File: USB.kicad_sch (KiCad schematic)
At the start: 51 parts, among them J3 USB_C_Receptacle_USB2.0, J4 USB_A_Stacked, Q4 BC817, U10 TPD4EUSB30, U4 CP2102N-Axx-xQFN24, U5 FSUSB30MUX, U6 FSUSB30MUX, U7 FE1.1, U8 TPD4EUSB30, U9 AP2191W, Y1 12MHz{slash}10pF

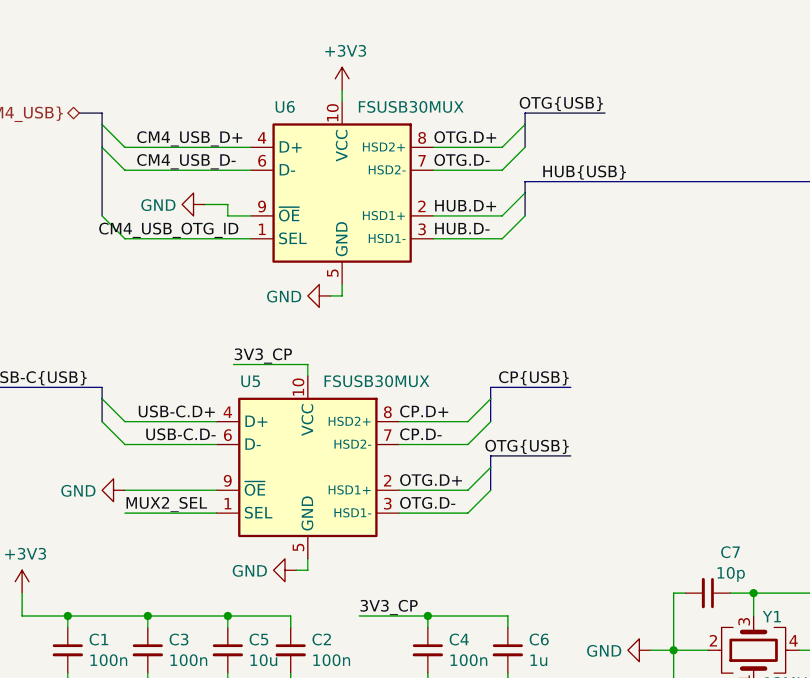
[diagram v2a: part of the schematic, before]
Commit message: Fix FSUSB30 Symbol and routing
Additionally a cap was added to U27.

Signed-off-by: Dominik Sliwa <dominik@sliwa.io>
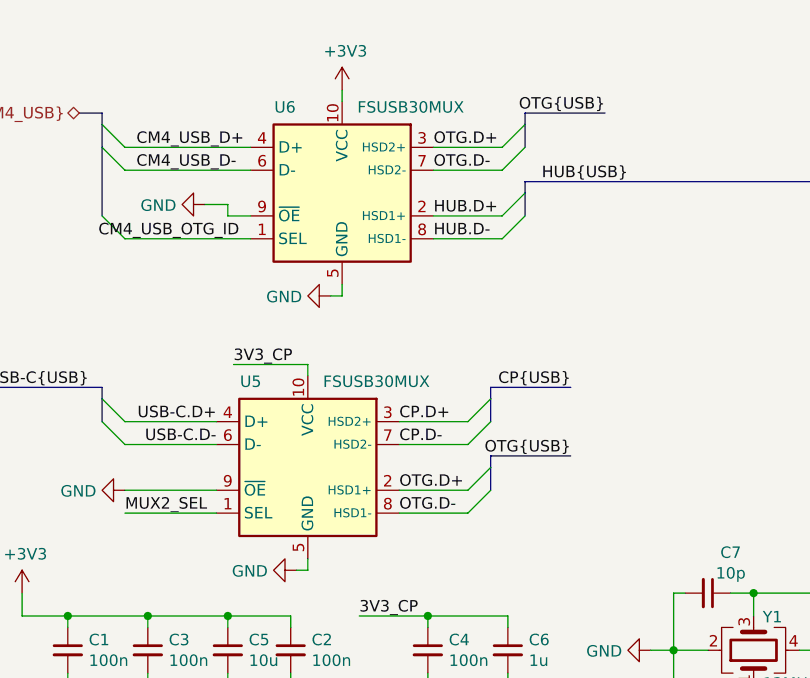
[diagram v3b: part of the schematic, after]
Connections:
- net CP.D+: now also U5.3 (HSD2+); no longer U5.8 (HSD2+)
- net HUB.D-: now also U6.8 (HSD1-); no longer U6.3 (HSD1-)
- net OTG.D+: now also U6.3 (HSD2+); no longer U6.8 (HSD2+)
- net OTG.D-: now also U5.8 (HSD1-); no longer U5.3 (HSD1-)
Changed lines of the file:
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@@
-(kicad_sch (version 20210621) (generator eeschema)
+(kicad_sch (version 20211123) (generator eeschema)
   (paper "A4")
   (title_block
@@
   (bus_alias "CM4_USB" (members "CM4_USB_D+" "CM4_USB_D-" "CM4_USB_OTG_ID"))
   (bus_alias "USB" (members "D+" "D-"))
-  (junction (at 40.64 88.9) (diameter 0.9144) (color 0 0 0 0))
-  (junction (at 92.075 154.305) (diameter 0.9144) (color 0 0 0 0))
-  (junction (at 143.51 29.21) (diameter 0.9144) (color 0 0 0 0))
-  (junction (at 22.86 80.01) (diameter 0.9144) (color 0 0 0 0))
-  (junction (at 228.6 42.545) (diameter 0) (color 0 0 0 0))
-  (junction (at 233.045 71.12) (diameter 0.9144) (color 0 0 0 0))
-  (junction (at 62.865 88.9) (diameter 0.9144) (color 0 0 0 0))
-  (junction (at 213.36 48.895) (diameter 0) (color 0 0 0 0))
-  (junction (at 92.075 139.065) (diameter 0.9144) (color 0 0 0 0))
-  (junction (at 152.4 29.21) (diameter 0.9144) (color 0 0 0 0))
-  (junction (at 274.32 123.19) (diameter 0.9144) (color 0 0 0 0))
-  (junction (at 144.78 100.33) (diameter 0.9144) (color 0 0 0 0))
-  (junction (at 238.125 34.29) (diameter 0.9144) (color 0 0 0 0))
-  (junction (at 215.265 59.69) (diameter 0.9144) (color 0 0 0 0))
-  (junction (at 222.885 89.535) (diameter 0.9144) (color 0 0 0 0))
-  (junction (at 62.865 80.01) (diameter 0.9144) (color 0 0 0 0))
-  (junction (at 224.155 71.12) (diameter 0.9144) (color 0 0 0 0))
-  (junction (at 149.86 29.21) (diameter 0.9144) (color 0 0 0 0))
-  (junction (at 215.265 71.12) (diameter 0.9144) (color 0 0 0 0))
-  (junction (at 47.625 88.9) (diameter 0.9144) (color 0 0 0 0))
-  (junction (at 36.83 194.945) (diameter 0.9144) (color 0 0 0 0))
-  (junction (at 31.75 80.01) (diameter 0.9144) (color 0 0 0 0))
-  (junction (at 119.38 72.39) (diameter 0.9144) (color 0 0 0 0))
-  (junction (at 40.64 80.01) (diameter 0.9144) (color 0 0 0 0))
-  (junction (at 135.89 139.7) (diameter 0.9144) (color 0 0 0 0))
-  (junction (at 163.83 29.21) (diameter 0.9144) (color 0 0 0 0))
-  (junction (at 92.075 163.195) (diameter 0.9144) (color 0 0 0 0))
-  (junction (at 119.38 55.88) (diameter 0.9144) (color 0 0 0 0))
-  (junction (at 234.315 34.29) (diameter 0) (color 0 0 0 0))
-  (junction (at 224.155 59.69) (diameter 0.9144) (color 0 0 0 0))
-  (junction (at 99.06 77.47) (diameter 0.9144) (color 0 0 0 0))
-  (junction (at 90.17 83.82) (diameter 0.9144) (color 0 0 0 0))
-  (junction (at 240.665 71.12) (diameter 0.9144) (color 0 0 0 0))
-  (junction (at 24.765 187.325) (diameter 0.9144) (color 0 0 0 0))
-  (junction (at 234.315 42.545) (diameter 0) (color 0 0 0 0))
-  (junction (at 92.075 147.955) (diameter 0.9144) (color 0 0 0 0))
-  (junction (at 22.86 88.9) (diameter 0.9144) (color 0 0 0 0))
-  (junction (at 31.75 88.9) (diameter 0.9144) (color 0 0 0 0))
-  (junction (at 135.89 144.78) (diameter 0.9144) (color 0 0 0 0))
-  (junction (at 170.18 69.85) (diameter 0.9144) (color 0 0 0 0))
-  (junction (at 224.155 98.425) (diameter 0.9144) (color 0 0 0 0))
-  (junction (at 230.505 34.29) (diameter 0.9144) (color 0 0 0 0))
-  (junction (at 173.99 19.685) (diameter 0.9144) (color 0 0 0 0))
-  (junction (at 123.19 132.08) (diameter 0.9144) (color 0 0 0 0))
-  (junction (at 240.665 59.69) (diameter 0.9144) (color 0 0 0 0))
-  (junction (at 53.975 179.705) (diameter 0.9144) (color 0 0 0 0))
-  (junction (at 163.83 19.685) (diameter 0.9144) (color 0 0 0 0))
-  (junction (at 234.315 24.13) (diameter 0.9144) (color 0 0 0 0))
-  (junction (at 99.06 90.17) (diameter 0.9144) (color 0 0 0 0))
-  (junction (at 233.045 59.69) (diameter 0.9144) (color 0 0 0 0))
+  (junction (at 215.265 71.12) (diameter 0.9144) (color 0 0 0 0)
+  )
+  (junction (at 31.75 80.01) (diameter 0.9144) (color 0 0 0 0)
+  )
+  (junction (at 92.075 139.065) (diameter 0.9144) (color 0 0 0 0)
+  )
+  (junction (at 40.64 80.01) (diameter 0.9144) (color 0 0 0 0)
+  )
+  (junction (at 149.86 29.21) (diameter 0.9144) (color 0 0 0 0)
+  )
+  (junction (at 213.36 48.895) (diameter 0) (color 0 0 0 0)
+  )
+  (junction (at 22.86 88.9) (diameter 0.9144) (color 0 0 0 0)
+  )
+  (junction (at 215.265 59.69) (diameter 0.9144) (color 0 0 0 0)
+  )
+  (junction (at 233.045 71.12) (diameter 0.9144) (color 0 0 0 0)
+  )
+  (junction (at 119.38 55.88) (diameter 0.9144) (color 0 0 0 0)
+  )
+  (junction (at 24.765 187.325) (diameter 0.9144) (color 0 0 0 0)
+  )
+  (junction (at 240.665 59.69) (diameter 0.9144) (color 0 0 0 0)
+  )
+  (junction (at 53.975 179.705) (diameter 0.9144) (color 0 0 0 0)
+  )
+  (junction (at 234.315 24.13) (diameter 0.9144) (color 0 0 0 0)
+  )
+  (junction (at 92.075 154.305) (diameter 0.9144) (color 0 0 0 0)
+  )
+  (junction (at 224.155 71.12) (diameter 0.9144) (color 0 0 0 0)
+  )
+  (junction (at 92.075 147.955) (diameter 0.9144) (color 0 0 0 0)
+  )
+  (junction (at 228.6 42.545) (diameter 0) (color 0 0 0 0)
+  )
+  (junction (at 173.99 19.685) (diameter 0.9144) (color 0 0 0 0)
+  )
+  (junction (at 234.315 42.545) (diameter 0) (color 0 0 0 0)
+  )
+  (junction (at 230.505 34.29) (diameter 0.9144) (color 0 0 0 0)
+  )
+  (junction (at 135.89 144.78) (diameter 0.9144) (color 0 0 0 0)
+  )
+  (junction (at 143.51 29.21) (diameter 0.9144) (color 0 0 0 0)
+  )
+  (junction (at 233.045 59.69) (diameter 0.9144) (color 0 0 0 0)
+  )
+  (junction (at 62.865 88.9) (diameter 0.9144) (color 0 0 0 0)
+  )
+  (junction (at 222.885 89.535) (diameter 0.9144) (color 0 0 0 0)
+  )
+  (junction (at 144.78 100.33) (diameter 0.9144) (color 0 0 0 0)
+  )
+  (junction (at 90.17 83.82) (diameter 0.9144) (color 0 0 0 0)
+  )
+  (junction (at 99.06 90.17) (diameter 0.9144) (color 0 0 0 0)
+  )
+  (junction (at 119.38 72.39) (diameter 0.9144) (color 0 0 0 0)
+  )
+  (junction (at 152.4 29.21) (diameter 0.9144) (color 0 0 0 0)
+  )
+  (junction (at 123.19 132.08) (diameter 0.9144) (color 0 0 0 0)
+  )
+  (junction (at 135.89 139.7) (diameter 0.9144) (color 0 0 0 0)
+  )
+  (junction (at 40.64 88.9) (diameter 0.9144) (color 0 0 0 0)
+  )
+  (junction (at 170.18 69.85) (diameter 0.9144) (color 0 0 0 0)
+  )
+  (junction (at 238.125 34.29) (diameter 0.9144) (color 0 0 0 0)
+  )
+  (junction (at 31.75 88.9) (diameter 0.9144) (color 0 0 0 0)
+  )
+  (junction (at 99.06 77.47) (diameter 0.9144) (color 0 0 0 0)
+  )
+  (junction (at 240.665 71.12) (diameter 0.9144) (color 0 0 0 0)
+  )
+  (junction (at 224.155 59.69) (diameter 0.9144) (color 0 0 0 0)
+  )
+  (junction (at 47.625 88.9) (diameter 0.9144) (color 0 0 0 0)
+  )
+  (junction (at 274.32 123.19) (diameter 0.9144) (color 0 0 0 0)
+  )
+  (junction (at 163.83 19.685) (diameter 0.9144) (color 0 0 0 0)
+  )
+  (junction (at 92.075 163.195) (diameter 0.9144) (color 0 0 0 0)
+  )
+  (junction (at 36.83 194.945) (diameter 0.9144) (color 0 0 0 0)
+  )
+  (junction (at 224.155 98.425) (diameter 0.9144) (color 0 0 0 0)
+  )
+  (junction (at 163.83 29.21) (diameter 0.9144) (color 0 0 0 0)
+  )
+  (junction (at 234.315 34.29) (diameter 0) (color 0 0 0 0)
+  )
+  (junction (at 62.865 80.01) (diameter 0.9144) (color 0 0 0 0)
+  )
+  (junction (at 22.86 80.01) (diameter 0.9144) (color 0 0 0 0)
+  )
   (no_connect (at 167.64 77.47))
   (no_connect (at 138.43 153.67))
@@
     (pin "3")
   )
-  (symbol (lib_id "Amber:FSUSB30MUX") (at 53.34 33.02 0) (unit 1)
+  (symbol (lib_name "FSUSB30MUX_1") (lib_id "Amber:FSUSB30MUX") (at 53.34 33.02 0) (unit 1)
     (in_bom yes) (on_board yes)
     (property "Reference" "U6" (id 0) (at 46.99 23.495 0))

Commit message: Rename Amber to Yellow everywhere
Signed-off-by: Stefan Agner <stefan@agner.ch>
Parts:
- J4: symbol Amber:USB_A_Stacked -> Yellow:USB_A_Stacked
- U10, U8: symbol Amber:TPD4EUSB30 -> Yellow:TPD4EUSB30
- U5, U6: symbol Amber:FSUSB30MUX -> Yellow:FSUSB30MUX
- U7: symbol Amber:FE1.1 -> Yellow:FE1.1
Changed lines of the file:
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@@
     (pin "3")
   )
-  (symbol (lib_name "FSUSB30MUX_1") (lib_id "Amber:FSUSB30MUX") (at 53.34 33.02 0) (unit 1)
+  (symbol (lib_name "FSUSB30MUX_1") (lib_id "Yellow:FSUSB30MUX") (at 53.34 33.02 0) (unit 1)
     (in_bom yes) (on_board yes)
     (property "Reference" "U6" (id 0) (at 46.99 23.495 0))
@@
     (pin "1")
   )
-  (symbol (lib_name "Amber:USB_A_Stacked_1") (lib_id "Amber:USB_A_Stacked") (at 264.16 81.28 0) (mirror y) (unit 1)
+  (symbol (lib_name "Yellow:USB_A_Stacked_1") (lib_id "Yellow:USB_A_Stacked") (at 264.16 81.28 0) (mirror y) (unit 1)
     (in_bom yes) (on_board yes)
     (property "Reference" "J4" (id 0) (at 261.62 68.58 0))
@@
     (pin "2")
   )
-  (symbol (lib_id "Amber:USB_A_Stacked") (at 264.16 113.03 0) (mirror y) (unit 2)
+  (symbol (lib_id "Yellow:USB_A_Stacked") (at 264.16 113.03 0) (mirror y) (unit 2)
     (in_bom yes) (on_board yes)
     (property "Reference" "J4" (id 0) (at 261.62 100.33 0))
@@
     (pin "2")
   )
-  (symbol (lib_id "Amber:TPD4EUSB30") (at 243.84 142.24 0) (unit 1)
+  (symbol (lib_id "Yellow:TPD4EUSB30") (at 243.84 142.24 0) (unit 1)
     (in_bom yes) (on_board yes)
     (property "Reference" "U10" (id 0) (at 243.84 129.54 0))
@@
     (pin "1")
   )
-  (symbol (lib_id "Amber:FE1.1") (at 144.78 64.77 0) (unit 1)
+  (symbol (lib_id "Yellow:FE1.1") (at 144.78 64.77 0) (unit 1)
     (in_bom yes) (on_board yes)
     (property "Reference" "U7" (id 0) (at 125.73 33.02 0))
@@
     (pin "2")
   )
-  (symbol (lib_id "Amber:FSUSB30MUX") (at 49.53 63.5 0) (unit 1)
+  (symbol (lib_id "Yellow:FSUSB30MUX") (at 49.53 63.5 0) (unit 1)
     (in_bom yes) (on_board yes)
     (property "Reference" "U5" (id 0) (at 43.18 53.975 0))
@@
     (pin "1")
   )
-  (symbol (lib_name "Amber:TPD4EUSB30_1") (lib_id "Amber:TPD4EUSB30") (at 152.4 181.61 0) (unit 1)
+  (symbol (lib_name "Yellow:TPD4EUSB30_1") (lib_id "Yellow:TPD4EUSB30") (at 152.4 181.61 0) (unit 1)
     (in_bom yes) (on_board yes)
     (property "Reference" "U8" (id 0) (at 152.4 168.91 0))

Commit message: Exclude TestPoints from BOM
Signed-off-by: Stefan Agner <stefan@agner.ch>
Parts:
- TP2, TP3: now left out of the parts list
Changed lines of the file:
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@@
   )
   (symbol (lib_id "Connector:TestPoint") (at 53.975 176.53 0) (unit 1)
-    (in_bom yes) (on_board yes) (fields_autoplaced)
+    (in_bom no) (on_board yes) (fields_autoplaced)
     (property "Reference" "TP3" (id 0) (at 56.007 174.0534 0)
       (effects (font (size 1.27 1.27)) (justify left))
@@
   )
   (symbol (lib_id "Connector:TestPoint") (at 36.83 190.5 0) (unit 1)
-    (in_bom yes) (on_board yes) (fields_autoplaced)
+    (in_bom no) (on_board yes) (fields_autoplaced)
     (property "Reference" "TP2" (id 0) (at 38.862 188.0234 0)
       (effects (font (size 1.27 1.27)) (justify left))

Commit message: Update PartNumber/Manufacturer
Fill in Manufacturer/PartNumber for the following parts:
- CP2102N-Axx-xQFN24
- FSUSB30MUX
- BC817

Signed-off-by: Stefan Agner <stefan@agner.ch>
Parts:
- Q4: Manufacturer (none) -> Nexperia USA; PartNumber (none) -> BC817-25,215
- U4: Manufacturer (none) -> Silicon Laboratories; PartNumber (none) -> CP2102N-A02-GQFN24
- U5: Manufacturer (none) -> ON Semiconductor; PartNumber (none) -> FSUSB30MUX
- U6: FielManufacturerd4 (none) -> ON Semiconductor; PartNumber (none) -> FSUSB30MUX
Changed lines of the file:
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@@
     (comment 2 "Yellow")
   )
+  (bus_alias "USB" (members "D+" "D-"))
+  (bus_alias "CM4_USB" (members "CM4_USB_D+" "CM4_USB_D-" "CM4_USB_OTG_ID"))
   (bus_alias "I2C" (members "SDA" "SCL"))
-  (bus_alias "CM4_USB" (members "CM4_USB_D+" "CM4_USB_D-" "CM4_USB_OTG_ID"))
-  (bus_alias "USB" (members "D+" "D-"))
   (junction (at 215.265 71.12) (diameter 0.9144) (color 0 0 0 0)
   )
@@
       (effects (font (size 1.27 1.27)) hide)
     )
+    (property "FielManufacturerd4" "ON Semiconductor" (id 4) (at 53.34 33.02 0)
+      (effects (font (size 1.27 1.27)) hide)
+    )
+    (property "PartNumber" "FSUSB30MUX" (id 5) (at 53.34 33.02 0)
+      (effects (font (size 1.27 1.27)) hide)
+    )
     (pin "1")
     (pin "10")
@@
     )
     (property "Config" "+AP2191" (id 4) (at 234.95 52.07 0))
+    (property "Manufacturer" "Nexperia USA" (id 5) (at 226.06 48.895 0)
+      (effects (font (size 1.27 1.27)) hide)
+    )
+    (property "PartNumber" "BC817-25,215" (id 6) (at 226.06 48.895 0)
+      (effects (font (size 1.27 1.27)) hide)
+    )
     (pin "1")
     (pin "2")
@@
       (effects (font (size 1.27 1.27)) hide)
     )
+    (property "Manufacturer" "Silicon Laboratories" (id 4) (at 45.72 133.985 0)
+      (effects (font (size 1.27 1.27)) hide)
+    )
+    (property "PartNumber" "CP2102N-A02-GQFN24" (id 5) (at 45.72 133.985 0)
+      (effects (font (size 1.27 1.27)) hide)
+    )
     (pin "1")
     (pin "10")
@@
       (effects (font (size 1.27 1.27)) hide)
     )
+    (property "Manufacturer" "ON Semiconductor" (id 4) (at 49.53 63.5 0)
+      (effects (font (size 1.27 1.27)) hide)
+    )
+    (property "PartNumber" "FSUSB30MUX" (id 5) (at 49.53 63.5 0)
+      (effects (font (size 1.27 1.27)) hide)
+    )

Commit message: Fix copy and paste error in Manufacturer property
Signed-off-by: Stefan Agner <stefan@agner.ch>
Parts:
- U6: FielManufacturerd4 ON Semiconductor -> (none); Manufacturer (none) -> ON Semiconductor
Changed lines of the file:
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@@
       (effects (font (size 1.27 1.27)) hide)
     )
-    (property "FielManufacturerd4" "ON Semiconductor" (id 4) (at 53.34 33.02 0)
+    (property "Manufacturer" "ON Semiconductor" (id 4) (at 53.34 33.02 0)
       (effects (font (size 1.27 1.27)) hide)
     )
